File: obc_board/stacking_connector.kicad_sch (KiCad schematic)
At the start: 37 parts, among them U5 LTC4304IMS#PBF, U6 PC104, U7 LTC4304IMS#PBF

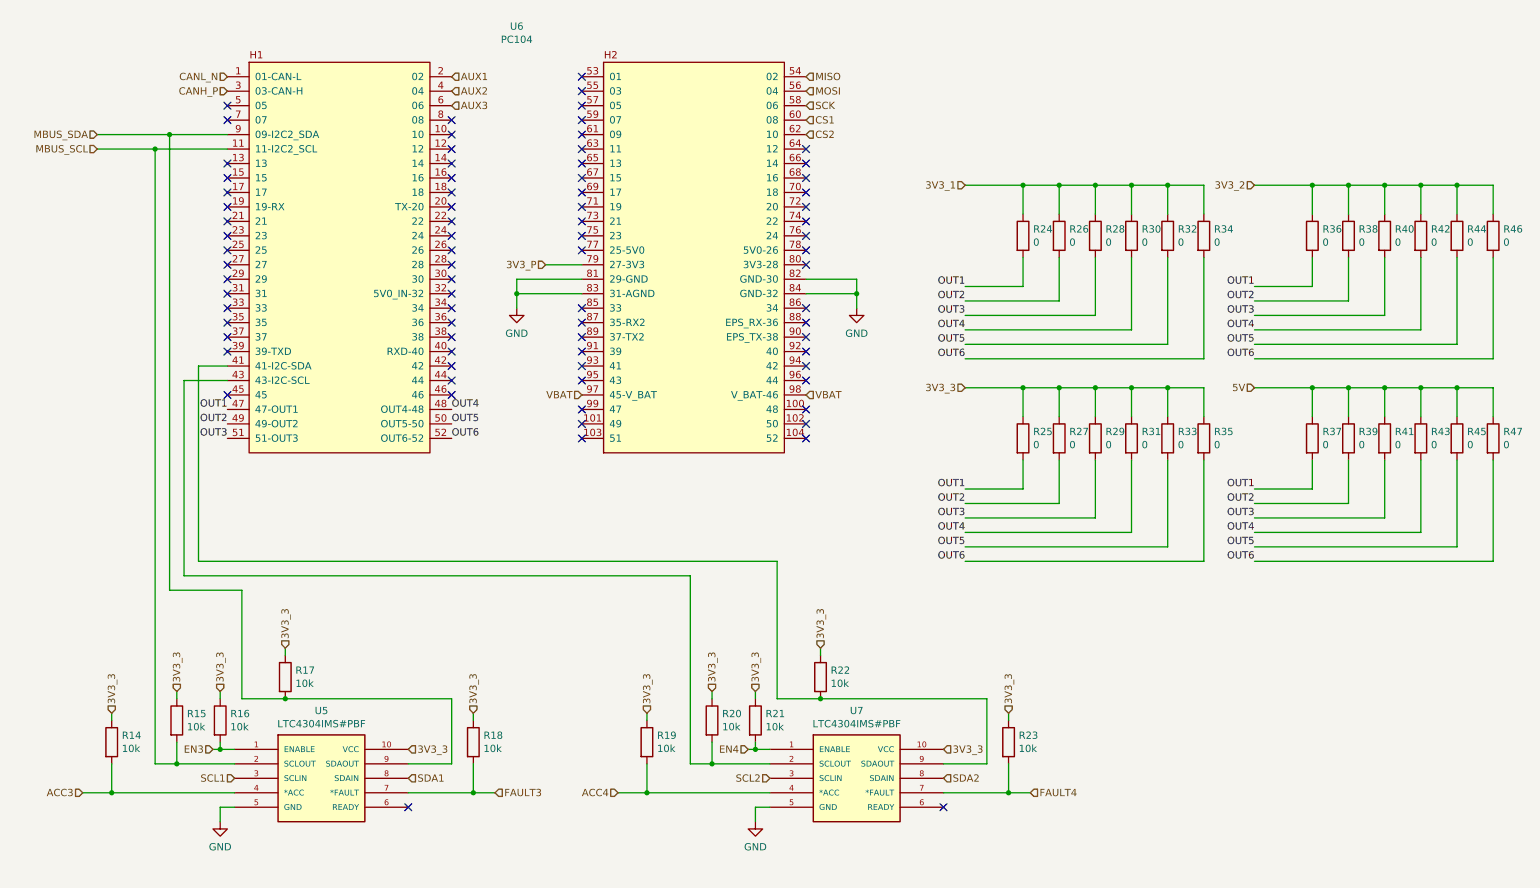
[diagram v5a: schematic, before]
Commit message: changed picoblade symbols to include mounting pins, added photodiode circuitry and additional testpoints, added GPS to FTDI jumper
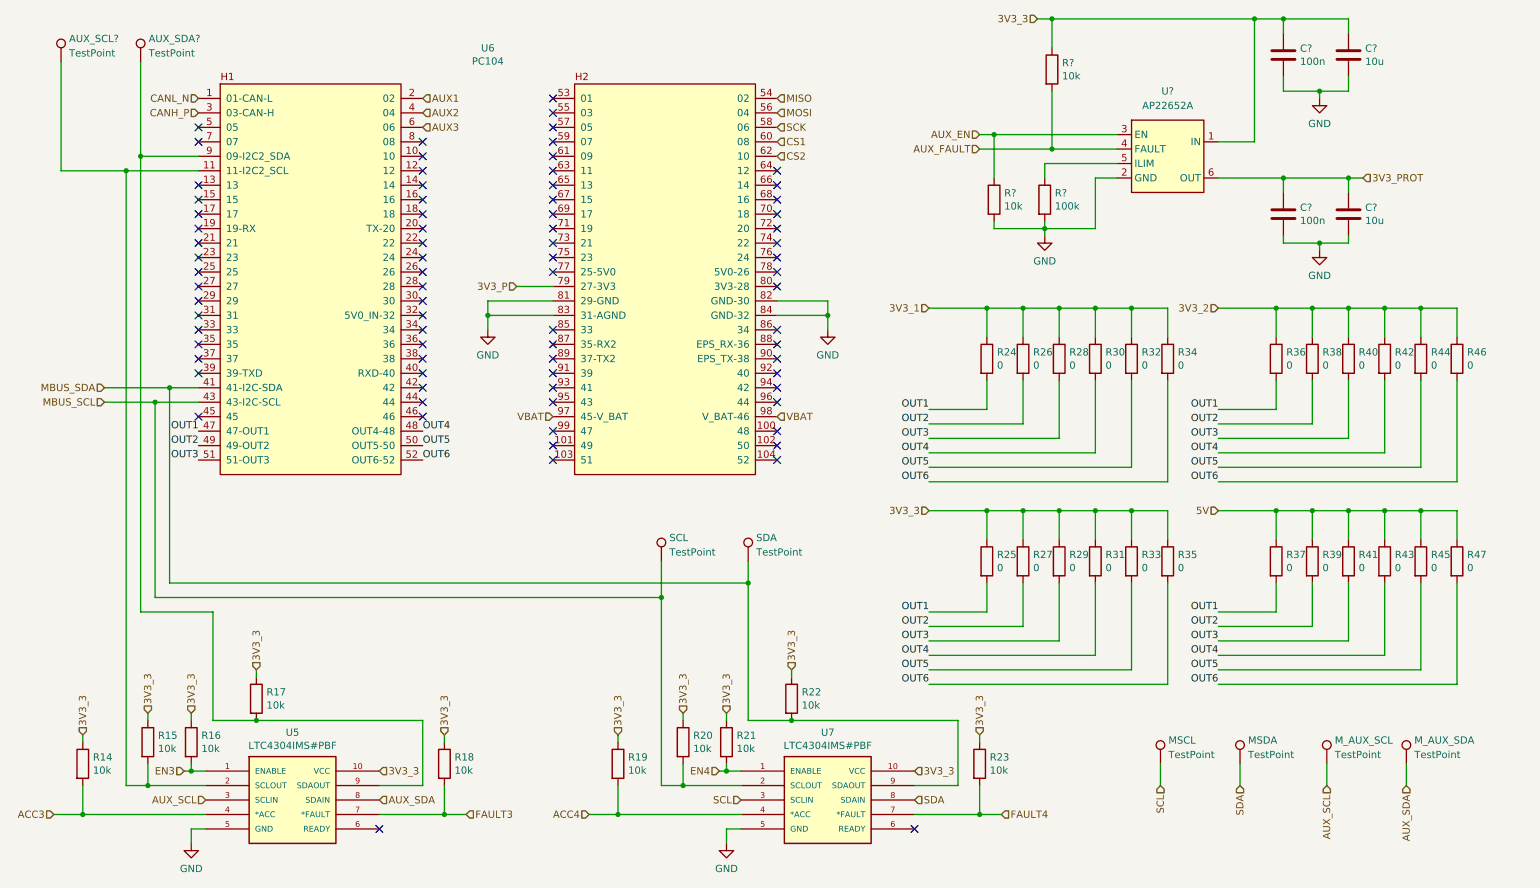
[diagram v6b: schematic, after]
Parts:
- added AUX_SCL?, AUX_SDA?, MSCL, MSDA, M_AUX_SCL, M_AUX_SDA, SCL, SDA: TestPoint, symbol Connector:TestPoint
- added C? (x2): 10u, Capacitor_SMD:C_1206_3216Metric, symbol Device:C
- added C? (x2): 100n, Capacitor_SMD:C_0402_1005Metric, symbol Device:C
- added R? (x2): 10k, Resistor_SMD:R_0402_1005Metric, symbol Device:R
- added R?: 100k, Resistor_SMD:R_0402_1005Metric, symbol Device:R
- added U?: AP22652A, Package_TO_SOT_SMD:SOT-23-6, symbol cubesat_obc_lib:AP22652A
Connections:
- net 3V3_3: now also C?.1, C?.1, R?.1, U?.1 (IN)
- net GND: now also C?.2, C?.2, C?.2, C?.2, R?.2, R?.2, U?.2 (GND)
- net MBUS_SCL: now also R20.2, U6.43 (43-I2C-SCL), U7.2 (SCLOUT), SCL.1; no longer R15.2, U5.2 (SCLOUT), U6.11 (11-I2C2_SCL)
- net MBUS_SDA: now also R22.2, U6.41 (41-I2C-SDA), U7.9 (SDAOUT), SDA.1; no longer R17.2, U5.9 (SDAOUT), U6.9 (09-I2C2_SDA)
- net SCL1 renamed AUX_SCL
- net AUX_SCL: now also M_AUX_SCL.1
- net SCL2 renamed SCL
- net SCL: now also MSCL.1
- net SDA1 renamed AUX_SDA
- net AUX_SDA: now also M_AUX_SDA.1
- net SDA2 renamed SDA
- net SDA: now also MSDA.1
- new net: AUX_SCL?.1, R15.2, U5.2 (SCLOUT), U6.11 (11-I2C2_SCL)
- new net: AUX_SDA?.1, R17.2, U5.9 (SDAOUT), U6.9 (09-I2C2_SDA)
- new net: R?.1, U?.5 (ILIM)
- new net 3V3_PROT: C?.1, C?.1, U?.6 (OUT)
- new net AUX_EN: R?.1, U?.3 (EN)
- new net AUX_FAULT: R?.2, U?.4 (FAULT)
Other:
- moved on the sheet: R14, R15, R16, R17, R18, R19, R20, R21, R22, R23, R24, R25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

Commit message: updated footprints
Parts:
- AUX_SCL?, AUX_SDA?, MSCL, MSDA, M_AUX_SCL, M_AUX_SDA, SCL, SDA: footprint (none) -> TestPoint:TestPoint_Pad_D1.5mm
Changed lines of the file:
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@@
       (effects (font (size 1.27 1.27)) (justify left))
     )
-    (property "Footprint" "" (id 2) (at 265.43 151.13 0)
+    (property "Footprint" "TestPoint:TestPoint_Pad_D1.5mm" (id 2) (at 265.43 151.13 0)
       (effects (font (size 1.27 1.27)) hide)
     )
@@
       (effects (font (size 1.27 1.27)) (justify left))
     )
-    (property "Footprint" "" (id 2) (at 222.25 151.13 0)
+    (property "Footprint" "TestPoint:TestPoint_Pad_D1.5mm" (id 2) (at 222.25 151.13 0)
       (effects (font (size 1.27 1.27)) hide)
     )
@@
       (effects (font (size 1.27 1.27)) (justify left))
     )
-    (property "Footprint" "" (id 2) (at 251.46 151.13 0)
+    (property "Footprint" "TestPoint:TestPoint_Pad_D1.5mm" (id 2) (at 251.46 151.13 0)
       (effects (font (size 1.27 1.27)) hide)
     )
@@
       (effects (font (size 1.27 1.27)) (justify left))
     )
-    (property "Footprint" "" (id 2) (at 43.18 27.94 0)
+    (property "Footprint" "TestPoint:TestPoint_Pad_D1.5mm" (id 2) (at 43.18 27.94 0)
       (effects (font (size 1.27 1.27)) hide)
     )
@@
       (effects (font (size 1.27 1.27)) (justify left))
     )
-    (property "Footprint" "" (id 2) (at 149.86 115.57 0)
+    (property "Footprint" "TestPoint:TestPoint_Pad_D1.5mm" (id 2) (at 149.86 115.57 0)
       (effects (font (size 1.27 1.27)) hide)
     )
@@
       (effects (font (size 1.27 1.27)) (justify left))
     )
-    (property "Footprint" "" (id 2) (at 134.62 115.57 0)
+    (property "Footprint" "TestPoint:TestPoint_Pad_D1.5mm" (id 2) (at 134.62 115.57 0)
       (effects (font (size 1.27 1.27)) hide)
     )
@@
       (effects (font (size 1.27 1.27)) (justify left))
     )
-    (property "Footprint" "" (id 2) (at 236.22 151.13 0)
+    (property "Footprint" "TestPoint:TestPoint_Pad_D1.5mm" (id 2) (at 236.22 151.13 0)
       (effects (font (size 1.27 1.27)) hide)
     )
@@
       (effects (font (size 1.27 1.27)) (justify left))
     )
-    (property "Footprint" "" (id 2) (at 29.21 27.94 0)
-      (effects (font (size 1.27 1.27)) hide)
-    )
+    (property "Footprint" "TestPoint:TestPoint_Pad_D1.5mm" (id 2) (at 29.21 27.94 0)
+      (effects (font (size 1.27 1.27)) hide)
+    )

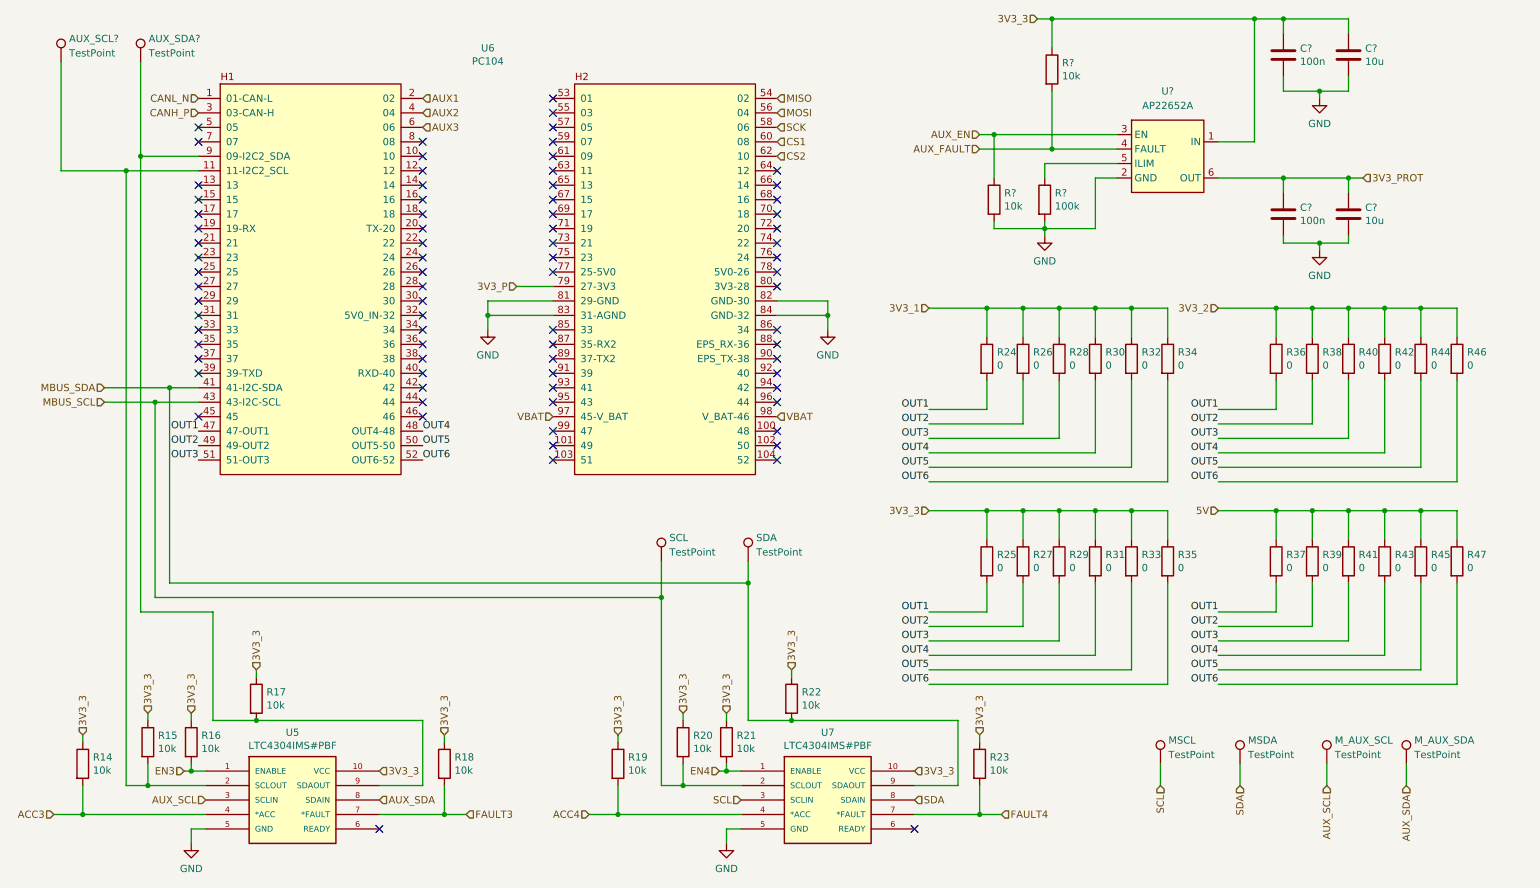
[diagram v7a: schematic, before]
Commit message: remapped magnetorquer pins, routed tespoints
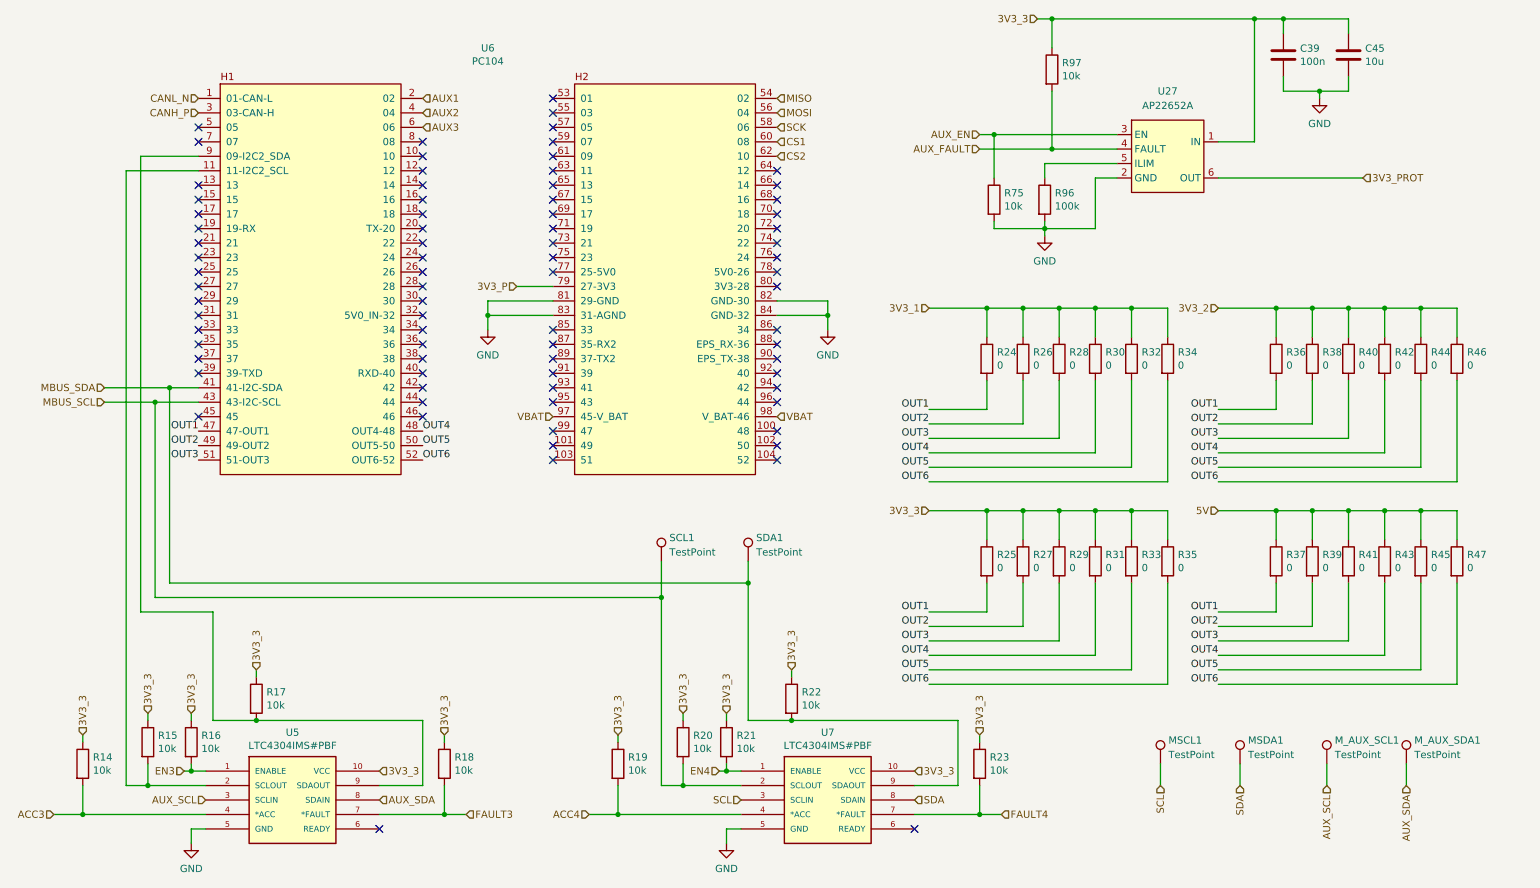
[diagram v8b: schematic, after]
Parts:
- removed AUX_SCL?, AUX_SDA?: TestPoint, TestPoint:TestPoint_Pad_D1.5mm, symbol Connector:TestPoint
- removed C?: 10u, Capacitor_SMD:C_1206_3216Metric, symbol Device:C
- removed C?: 100n, Capacitor_SMD:C_0402_1005Metric, symbol Device:C
- MSCL1: renamed from MSCL; footprint TestPoint:TestPoint_Pad_D1.5mm -> TestPoint:TestPoint_Pad_D1.0mm
- MSDA1: renamed from MSDA; footprint TestPoint:TestPoint_Pad_D1.5mm -> TestPoint:TestPoint_Pad_D1.0mm
- M_AUX_SCL1: renamed from M_AUX_SCL; footprint TestPoint:TestPoint_Pad_D1.5mm -> TestPoint:TestPoint_Pad_D1.0mm
- M_AUX_SDA1: renamed from M_AUX_SDA; footprint TestPoint:TestPoint_Pad_D1.5mm -> TestPoint:TestPoint_Pad_D1.0mm
- SCL1: renamed from SCL; footprint TestPoint:TestPoint_Pad_D1.5mm -> TestPoint:TestPoint_Pad_D1.0mm
- SDA1: renamed from SDA; footprint TestPoint:TestPoint_Pad_D1.5mm -> TestPoint:TestPoint_Pad_D1.0mm
- gave numbers to parts that had none: 6
